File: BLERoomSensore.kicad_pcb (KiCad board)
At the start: 2 copper layers, 33.9 x 22.3 mm, 7 parts, among them J1 FTSH-105-01-F-DV-P-TR, U2 BME280, U3 BMD-360-A-R

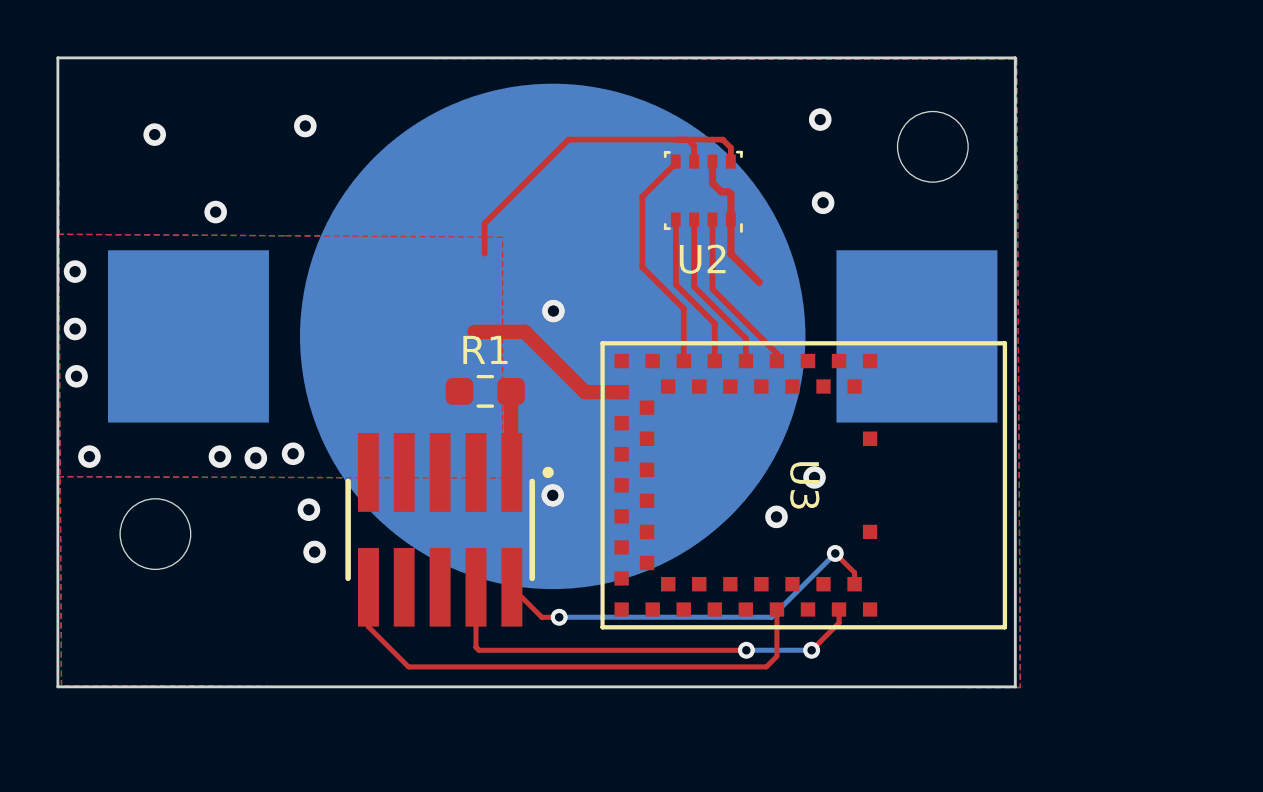
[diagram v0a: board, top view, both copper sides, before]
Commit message: Routing Done, no DRC errors
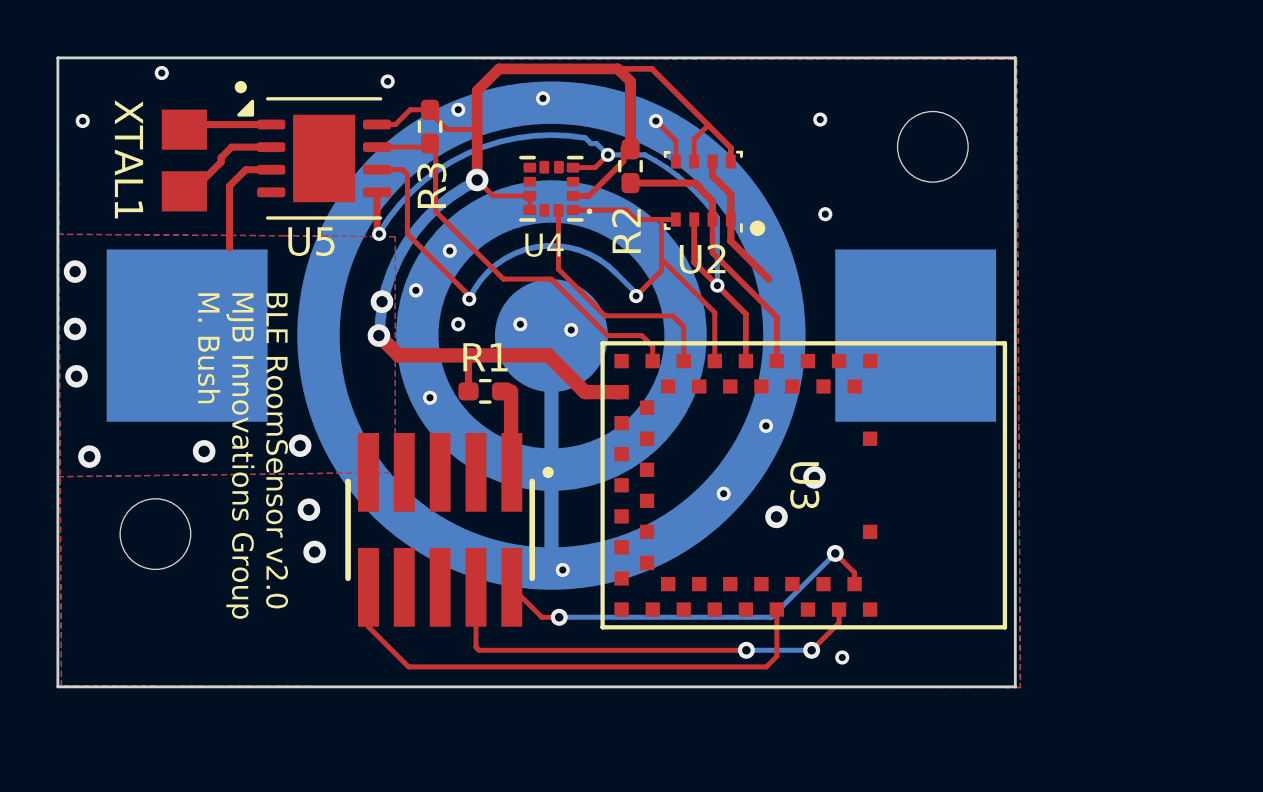
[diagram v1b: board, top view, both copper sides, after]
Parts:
- added R2: 10k, Resistor_SMD:R_0402_1005Metric_Pad0.72x0.64mm_HandSolder, F.Cu at (142.2, 71.4)
- added R3: 10k, Resistor_SMD:R_0402_1005Metric_Pad0.72x0.64mm_HandSolder, F.Cu at (135.1, 70.0)
- added U4: LIS2DH12TR, LIS2DH12TR:PQFN50P200X200100-12N, F.Cu at (139.4, 72.2)
- added U5: PCF8523TK, Package_SON:HVSON-8-1EP_4x4mm_P0.8mm_EP2.2x3.1mm, F.Cu at (131.3, 71.1)
- added XTAL1: FC-135 32.7680KA-A3, FC_135_32_7680KA_A3:XTAL_FC-135R_EPS, F.Cu at (126.4, 71.2)
- BT1: value BAT-HLD-003-SMT -> Battery_Cell; footprint BAT_HLD_003_SMT:BAT_BAT-HLD-003-SMT -> BAT_HLD_003_SMT:BAT_BAT-HLD-003-SMT_MOD
- R1: footprint Resistor_SMD:R_0603_1608Metric_Pad0.98x0.95mm_HandSolder -> Resistor_SMD:R_0402_1005Metric_Pad0.72x0.64mm_HandSolder
- moved BT1 0.05 mm to (139.4, 77.4)
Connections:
- net MOSI renamed SDA
- net SCK renamed SCL
- U2 pad 5: MISO -> GND
- U3 pad 13: MISO -> LIS_INT
- U3 pad 15: unconnected-(U3-P0.02-Pad15) -> PCF_INT
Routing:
- net VDD: track 19.1 -> 43.4 mm, vias 7 -> 9
- net PCF_INT: track 0.00 -> 14.6 mm
- net SCL: track 5.64 -> 18.8 mm, vias 0 -> 2
- net SDA: track 5.83 -> 16.9 mm, vias 0 -> 3
- net LIS_INT: track 0.00 -> 8.58 mm
- net MISO: track 8.11 -> 0.00 mm
- net BME_CS: track 6.01 -> 9.85 mm
- net Net-(U5-OSCO): track 0.00 -> 3.82 mm
- net Net-(U5-OSCI): track 0.00 -> 2.65 mm
- net GND: track 5.06 -> 6.66 mm, vias 11 -> 22
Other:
- board text added: "BLE RoomSensor v2.0 MJB Innovations Group M. Bush"

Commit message: Add expansion header
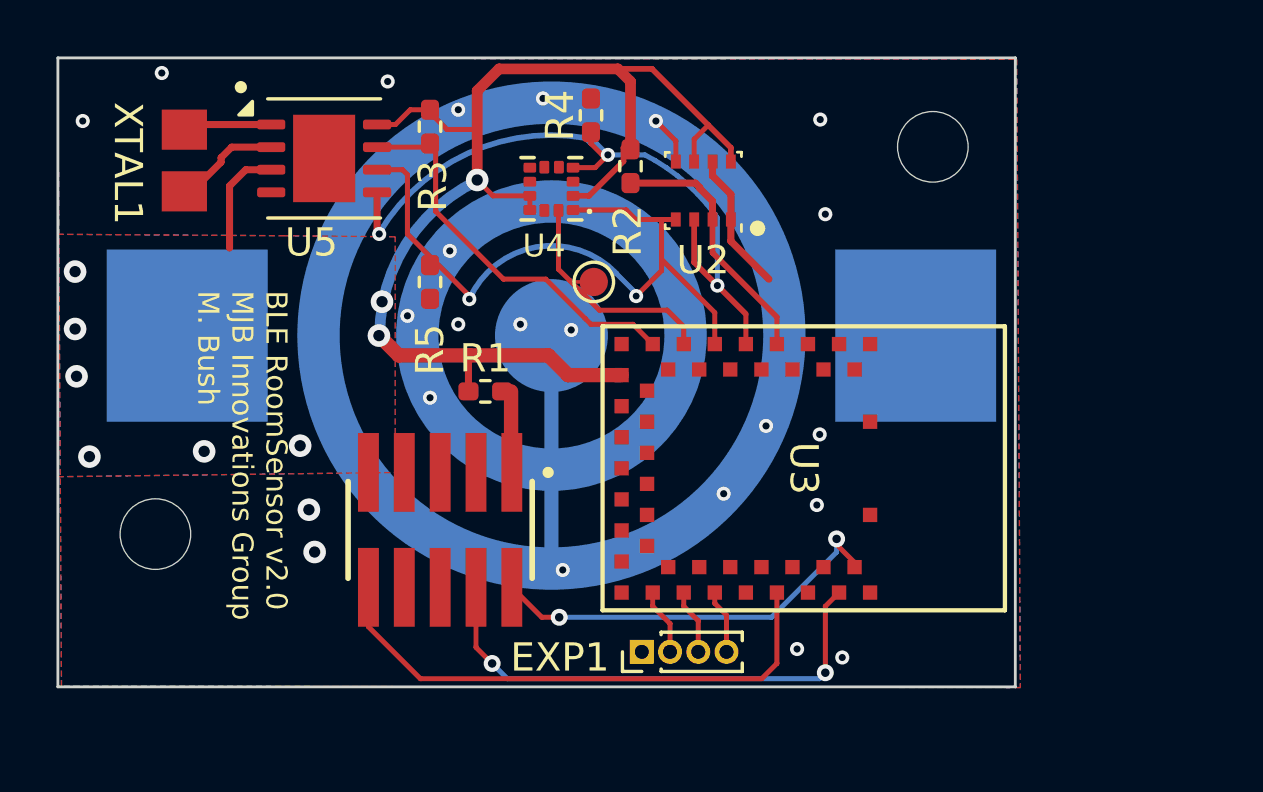
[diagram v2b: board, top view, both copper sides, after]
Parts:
- added EXP1: Conn_01x04_Pin, Connector_PinHeader_1.00mm:PinHeader_1x04_P1.00mm_Vertical, F.Cu at (142.6, 88.6)
- added R4: 10k, Resistor_SMD:R_0402_1005Metric_Pad0.72x0.64mm_HandSolder, F.Cu at (140.8, 69.6)
- added R5: 10k, Resistor_SMD:R_0402_1005Metric_Pad0.72x0.64mm_HandSolder, F.Cu at (135.1, 75.5)
- added TP_LIS1: TestPoint, TestPoint:TestPoint_Pad_D1.0mm, F.Cu at (140.9, 75.5)
- R1: value 10k -> 0
- R2, R3: value 10k -> 100k
- moved U3 0.60 mm to (148.3, 82.1)
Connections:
- U3 pad 31: unconnected-(U3-P0.13-Pad31) -> Net-(EXP1-Pin_2)
- U3 pad 33: unconnected-(U3-P0.15-Pad33) -> Net-(EXP1-Pin_3)
- U3 pad 35: unconnected-(U3-P0.17-Pad35) -> Net-(EXP1-Pin_4)
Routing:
- net Net-(EXP1-Pin_2): track 0.00 -> 2.35 mm
- net Net-(EXP1-Pin_3): track 0.00 -> 2.31 mm
- net Net-(EXP1-Pin_4): track 0.00 -> 2.27 mm
- net CLK: track 15.9 -> 18.1 mm
- net RESET: track 18.3 -> 19.4 mm
- net SCL: track 18.8 -> 18.2 mm
- net BME_CS: track 9.85 -> 9.25 mm
- net SDA: track 16.9 -> 17.5 mm
- net PCF_INT: track 14.6 -> 14.0 mm
- net GND: vias 22 -> 23

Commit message: BOM
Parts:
- moved R3 1.00 mm to (135.7, 70.8)

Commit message: Bunch o production files
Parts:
- removed J1: FTSH-105-01-F-DV-P-TR, FTSH-105-01-F-DV-P-TR:SAMTEC_FTSH-105-01-F-DV-P-TR
- added J2: Conn_ARM_SWD_TagConnect_TC2030-NL, Connector:Tag-Connect_TC2030-IDC-NL_2x03_P1.27mm_Vertical, F.Cu at (135.4, 87.5)
- U5: value PCF8523TK -> PCF8523T; footprint Package_SON:HVSON-8-1EP_4x4mm_P0.8mm_EP2.2x3.1mm -> Package_SO:SOIC-8_3.9x4.9mm_P1.27mm
- moved R1 5.18 mm to (137.8, 84.5), turned to 180 degrees
- moved XTAL1 1.30 mm to (125.1, 71.1)
- moved U5 1.16 mm to (130.2, 71.0)
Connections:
- R1 pad 1: VDD -> Net-(J2-VCC)
- R1 pad 2: Net-(J1-Pad01) -> VDD
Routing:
- net VDD: track 43.1 -> 51.8 mm
- net Net-(J2-VCC): track 0.00 -> 3.08 mm
- net RESET: track 19.4 -> 16.4 mm
- net Net-(J1-Pad01): track 2.88 -> 0.00 mm
- net DIO: track 14.5 -> 16.0 mm
- net GND: vias 23 -> 25

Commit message: Working on comp changes
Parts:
- removed U3: BMD-360-A-R, BMD_360_A_R:BMD-360_UBL
- added AE1: 2450AT18A100E, Capacitor_SMD:C_0603_1608Metric, F.Cu at (160.9, 83.6)
- added C1: 100nF X7S, Capacitor_SMD:C_0402_1005Metric_Pad0.74x0.62mm_HandSolder, F.Cu at (145.4, 79.6)
- added C10: 4.7uF X7R, Capacitor_SMD:C_0603_1608Metric_Pad1.08x0.95mm_HandSolder, F.Cu at (143.9, 83.9)
- added C11: 1pF NP0, Capacitor_SMD:C_0402_1005Metric_Pad0.74x0.62mm_HandSolder, F.Cu at (155.9, 85.3)
- added C12: 1.2pF NP0, Capacitor_SMD:C_0402_1005Metric_Pad0.74x0.62mm_HandSolder, F.Cu at (157.7, 85.3)
- added C2: 100nF X7S, Capacitor_SMD:C_0402_1005Metric_Pad0.74x0.62mm_HandSolder, F.Cu at (150.8, 86.8)
- added C3: 100nF X7S, Capacitor_SMD:C_0402_1005Metric_Pad0.74x0.62mm_HandSolder, F.Cu at (153.0, 77.7)
- added C4: 100nF X7S, Capacitor_SMD:C_0402_1005Metric_Pad0.74x0.62mm_HandSolder, F.Cu at (153.7, 85.5)
- added C5: 0.1uF X7S, Capacitor_SMD:C_0402_1005Metric_Pad0.74x0.62mm_HandSolder, F.Cu at (156.0, 81.8)
- added C6: 0.1uF X7S, Capacitor_SMD:C_0402_1005Metric_Pad0.74x0.62mm_HandSolder, F.Cu at (148.0, 77.6)
- added C7: 100pF NP0, Capacitor_SMD:C_0402_1005Metric_Pad0.74x0.62mm_HandSolder, F.Cu at (156.0, 80.8)
- added C8: 12pF NP0, Capacitor_SMD:C_0402_1005Metric_Pad0.74x0.62mm_HandSolder, F.Cu at (157.0, 79.1)
- added C9: 12pF NP0, Capacitor_SMD:C_0402_1005Metric_Pad0.74x0.62mm_HandSolder, F.Cu at (157.0, 75.1)
- added L1: 4.7nH, Inductor_SMD:L_0402_1005Metric, F.Cu at (156.4, 83.6)
- added L2: 2.2nH, Inductor_SMD:L_0402_1005Metric, F.Cu at (158.4, 83.6)
- added U1: nRF52833_QDxx, Package_DFN_QFN:QFN-40-1EP_5x5mm_P0.4mm_EP3.6x3.6mm, F.Cu at (149.9, 82.2)
- added Y1: X201632MOB4SI, Crystal:Crystal_SMD_2016-4Pin_2.0x1.6mm, F.Cu at (157.0, 77.1)
- EXP1: footprint Connector_PinHeader_1.00mm:PinHeader_1x04_P1.00mm_Vertical -> Connector_PinHeader_1.27mm:PinHeader_1x04_P1.27mm_Vertical
- moved EXP1 2.10 mm to (144.7, 88.1)
- moved J2 1.03 mm to (136.4, 87.9)
- moved R1 0.33 mm to (137.7, 84.2), turned to 90 degrees
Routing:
- net VDD: track 51.8 -> 70.9 mm, vias 9 -> 13
- net DEC4_6: track 0.00 -> 11.6 mm, vias 0 -> 2
- net PCF_INT: track 14.5 -> 3.45 mm
- net Net-(U1-XC2): track 0.00 -> 8.62 mm
- net Net-(U1-XC1): track 0.00 -> 7.69 mm
- net BME_CS: track 9.25 -> 3.84 mm
- net LIS_INT: track 8.85 -> 3.52 mm
- net Net-(U1-ANT): track 0.00 -> 5.20 mm
- net DIO: track 16.0 -> 20.3 mm
- net SCL: track 18.5 -> 14.7 mm
- net DEC3: track 0.00 -> 3.42 mm
- net Net-(EXP1-Pin_2): track 2.35 -> 5.46 mm
- net CLK: track 17.9 -> 20.9 mm
- net Net-(EXP1-Pin_3): track 2.31 -> 4.92 mm
- net Net-(EXP1-Pin_4): track 2.27 -> 4.81 mm
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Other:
- board size 33.9 x 22.3 mm -> 40.6 x 22.3 mm
